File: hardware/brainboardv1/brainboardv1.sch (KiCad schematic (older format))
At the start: 15 parts, among them P1 WP, P5 GND, P6 5VD, P7 3V3, U1 24C256, U2 BEAGLEBONE_BLACK

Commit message: Nearly finished v1 sch & brd, await final check
Fixed errors from Rev 0, added MPU-6050 accelerometer/gyro for head
motion tracking, switched to +/-2.5V analog supply, added 2 bipolar
analog inputs for EOG tracking, added daisy-chain capability
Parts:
- removed P6: 5VD, ~, symbol TST
- SJ4: value SOLDERJUMPERNC2 -> A2
- SJ5: value SOLDERJUMPERNC2 -> A1
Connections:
- net labels added: /CS_DAISY, /CS_MAIN, /DRDY, /PWDN, CLK, I2C2_SCL, I2C2_SDA, MISO, MOSI, SCLK, UARTBT_CTS, UARTBT_RTS
- net labels removed: +5VD, 3V3, AGND, GNDPWR, SYS_RESETn
- wire segments 62 -> 63
- no-connect marks 71 -> 64
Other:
- note added: "If using MCU for Bluetooth communications, make sure BBB\nUART1 RX/TX/RTS/CTS are configured as inputs to prevent\nbus contention!"
- note added: "UART2_TXD/RXD mux config to MODE2 (I2C2_SCL/SDA),\nI2C2_SCL/SDA mux config to MODE0 (UART1_RTSN/CTSN)\n"
- note added: "UARTBT on BBB UART1,\nUARTUC on BBB UART4"
- moved on the sheet: P1, P5, R1, R2, R3, R4, R5, R6, S2, SJ4, SJ5, U1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

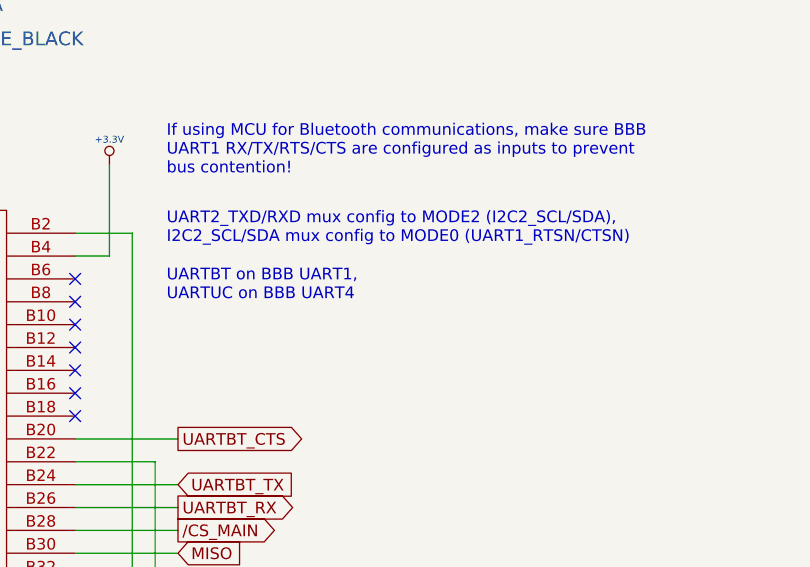
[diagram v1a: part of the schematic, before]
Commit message: Added thicker power traces and fixed silkscreen
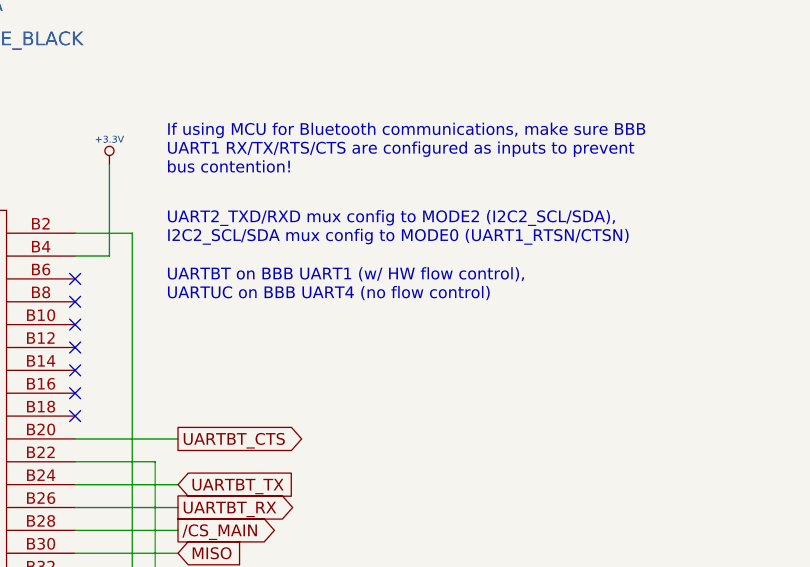
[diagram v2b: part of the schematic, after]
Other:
- note added: "UARTBT on BBB UART1 (w/ HW flow control),\nUARTUC on BBB UART4 (no flow control)"
- note removed: "UARTBT on BBB UART1,\nUARTUC on BBB UART4"
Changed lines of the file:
@@
 Sheet 1 7
 Title "BrainBoard: Open-Source Hardware for Wearable BCI"
-Date "27 dec 2013"
+Date "30 dec 2013"
 Rev "0"
 Comp "Virginia Commonwealth University"
@@
 NoConn ~ 8950 2600
 Text Notes 8800 4500 0    51   ~ 0
-UARTBT on BBB UART1,\nUARTUC on BBB UART4
+UARTBT on BBB UART1 (w/ HW flow control),\nUARTUC on BBB UART4 (no flow control)
 NoConn ~ 8400 4600
 Connection ~ 5900 6700
